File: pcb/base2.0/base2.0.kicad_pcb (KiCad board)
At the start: 4 copper layers, 24 x 24 mm, 32 parts, among them J1 Conn_01x01_Male, J2 Conn_01x01_Male, J3 Conn_01x04_Male, J4 Conn_01x02_Male, U1 STM32G431CBU6, U2 tile, U3 AP2210-33, U4 MPU-9250

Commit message: le update
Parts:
- removed R10, R6, R7, R8, R9: 10k, Resistor_SMD:R_0402_1005Metric
- C9: value 0.1uF -> 100nf
- U4: value MPU-9250 -> LSM6DS3; footprint Sensor_Motion:InvenSense_QFN-24_3x3mm_P0.4mm -> Package_LGA:LGA-14_3x2.5mm_P0.5mm_LayoutBorder3x4y
- moved C9 1.65 mm to (202.9, 101.1), turned to 180 degrees
- moved C8 1.01 mm to (204.9, 101.1), turned to 180 degrees
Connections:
- C8 pad 1: GND -> +3V3
- C8 pad 2: +3V3 -> GND
- C9 pad 1: Net-(C9-Pad1) -> GND
- C9 pad 2: GND -> +3V3
- U4 pad 1: +3V3 -> GND
- U4 pad 10: Net-(C9-Pad1) -> Net-(U4-Pad10)
- U4 pad 12: Net-(R10-Pad1) -> +3V3
- U4 pad 13: +3V3 -> I2C_SCL
- U4 pad 14: (no net) -> I2C_SDA
- U4 pad 2: (no net) -> GND
- U4 pad 3: (no net) -> GND
- U4 pad 4: (no net) -> Net-(U4-Pad4)
- U4 pad 5: (no net) -> +3V3
- U4 pad 6: (no net) -> GND
- U4 pad 7: I2C_SCL -> GND
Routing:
- net GND: track 23.8 -> 30.2 mm, vias 5 -> 14
- net I2C_SCL: track 15.0 -> 18.7 mm
- net Net-(R10-Pad1): track 2.86 -> 0.00 mm
- net I2C_SDA: track 18.0 -> 15.5 mm
- net Net-(U4-Pad11): track 2.31 -> 0.00 mm
- net Net-(C9-Pad1): track 2.27 -> 0.00 mm
- net Net-(R8-Pad2): track 1.83 -> 0.00 mm
- net Net-(U4-Pad9): track 1.80 -> 0.00 mm
- net Net-(R6-Pad2): track 1.57 -> 0.00 mm
- net +3V3: track 40.3 -> 40.5 mm, vias 14 -> 13

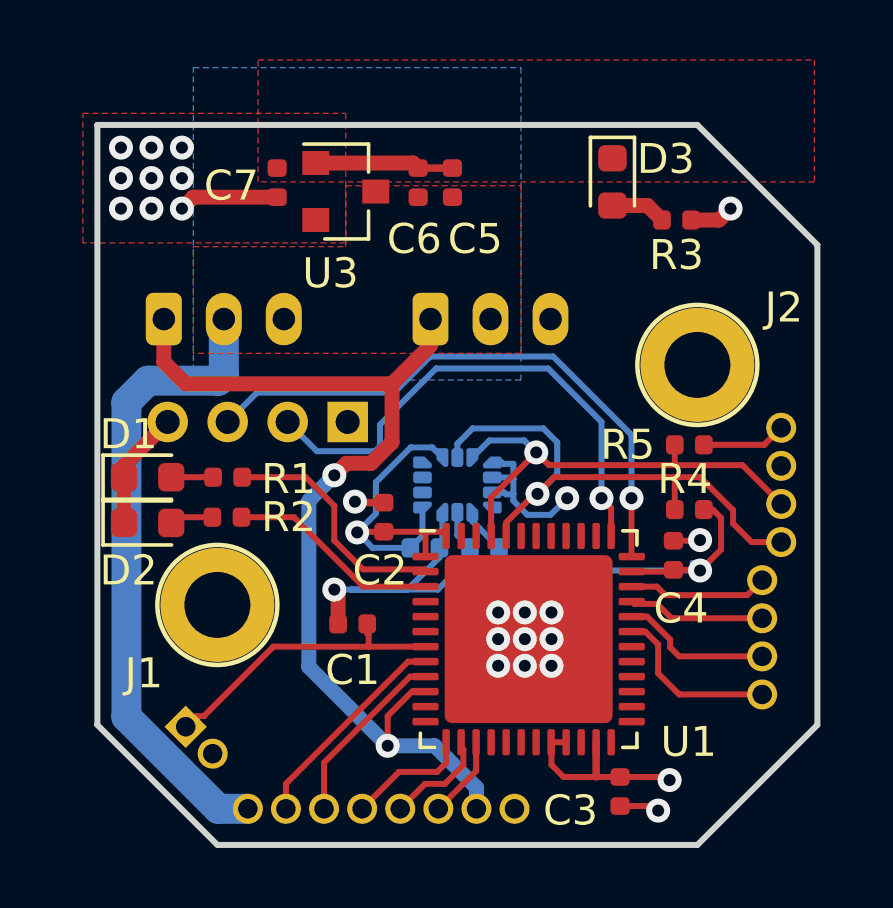
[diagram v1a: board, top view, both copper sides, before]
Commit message: Small changes to base pcb
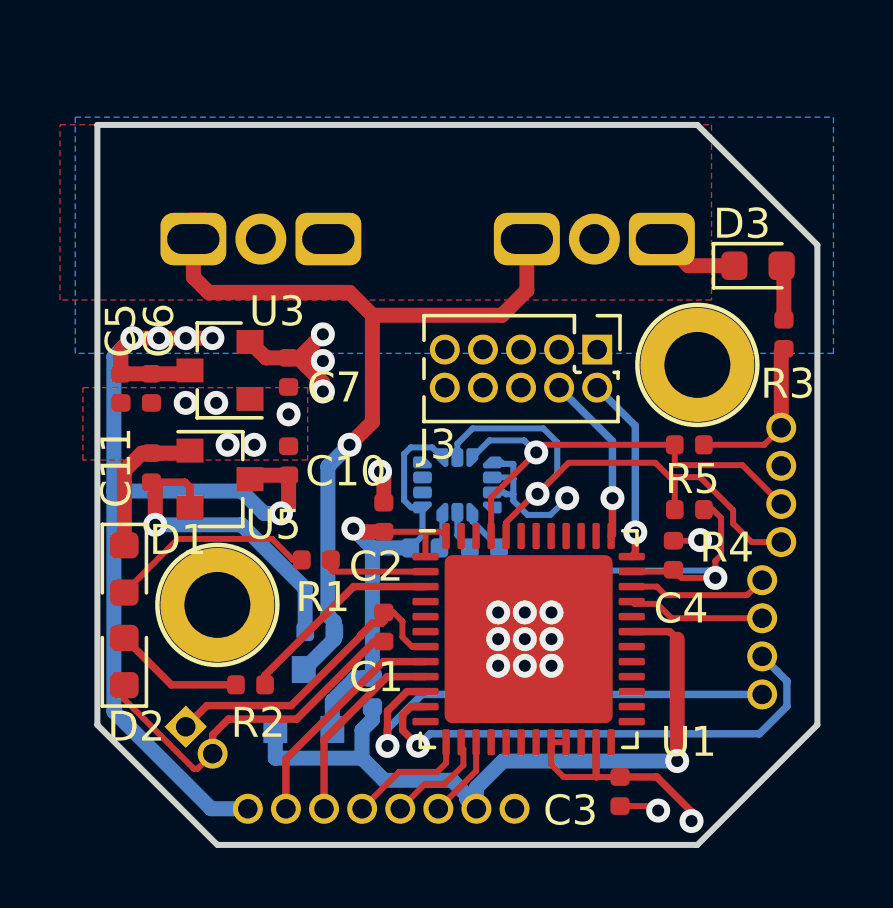
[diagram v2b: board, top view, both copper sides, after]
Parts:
- added C10: 1uf, Capacitor_SMD:C_0402_1005Metric, F.Cu at (198.4, 98.2)
- added C11: 2.2uF, Capacitor_SMD:C_0402_1005Metric, F.Cu at (193.8, 98.4)
- added Q1: BSS123, Package_TO_SOT_SMD:SOT-23, B.Cu at (198.9, 106.2)
- added R6: 10k, Resistor_SMD:R_0402_1005Metric, B.Cu at (199.4, 103.9)
- added R7: 10k, Resistor_SMD:R_0402_1005Metric, B.Cu at (201.2, 105.9)
- added U5: AP2210-5, Package_TO_SOT_SMD:SOT-23, F.Cu at (196.1, 98.8)
- J3: value Conn_01x04_Male -> Conn_ARM_JTAG_SWD_10; footprint Connector_PinHeader_2.00mm:PinHeader_1x04_P2.00mm_Vertical -> Connector_PinHeader_1.27mm:PinHeader_2x05_P1.27mm_Vertical; moved to F.Cu
- S1, S2: footprint Connector_JST:JST_PH_S3B-PH-K_1x03_P2.00mm_Horizontal -> tile:jst_bus_horizontal
- moved C5 13.0 mm to (192.8, 95.8), turned to 270 degrees
- moved C6 11.2 mm to (193.8, 95.8), turned to 270 degrees
- moved J3 8.66 mm to (208.7, 94.5), turned to 270 degrees
- moved S2 7.92 mm to (210.6, 90.8), turned to 180 degrees
- moved U3 7.29 mm to (196.1, 95.2), turned to 180 degrees
- moved C7 6.34 mm to (198.4, 95.2), turned to 270 degrees
- moved S1 5.87 mm to (199.4, 90.8), turned to 180 degrees
- moved R2 5.64 mm to (197.1, 105.7)
- moved D3 5.60 mm to (214.0, 91.7), turned to 0 degrees
- moved R3 5.23 mm to (214.9, 94.0), turned to 90 degrees
- moved D2 4.69 mm to (192.9, 104.9), turned to 90 degrees
- moved R1 4.04 mm to (199.3, 101.5)
- moved D1 3.15 mm to (192.9, 101.8), turned to 270 degrees
- moved C1 1.04 mm to (201.5, 103.7), turned to 270 degrees
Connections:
- J3 pad 2: JTCK-SWCLI -> JTMS-SWDIO
- J3 pad 3: JTMS-SWDIO -> GND
- J3 pad 4: GND -> JTCK-SWCLI
- S1 pad 1: USART2 -> GND
- S1 pad 3: GND -> USART1_5
- S2 pad 1: USART2 -> GND
- S2 pad 3: GND -> USART1_5
- U1 pad 10: USART2 -> USART2_TX
- U1 pad 11: Net-(U1-Pad11) -> USART2_RX
- U1 pad 31: USART1_TX -> USART1_3
- U1 pad 32: USART1_RX -> Net-(U1-Pad32)
- U1 pad 44: I2C_SCL -> Net-(U1-Pad44)
- U1 pad 46: Net-(U1-Pad46) -> I2C_SCL
- U2 pad 10: USART2 -> USART1_3
- U2 pad 7: USART1_RX -> USART2_RX
- U2 pad 8: USART1_TX -> USART2_TX
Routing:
- net USART2: track 33.6 -> 0.00 mm, vias 2 -> 0
- net USART1_5: track 0.00 -> 28.4 mm, vias 0 -> 1
- net USART1_3: track 0.00 -> 23.7 mm, vias 0 -> 1
- net USART2_RX: track 0.00 -> 17.0 mm, vias 0 -> 1
- net USART2_TX: track 0.00 -> 16.2 mm, vias 0 -> 1
- net +3V3: track 40.5 -> 53.9 mm, vias 13 -> 6
- net JTMS-SWDIO: track 19.5 -> 6.21 mm
- net VCC: track 21.3 -> 33.6 mm, vias 0 -> 5
- net JTCK-SWCLI: track 17.1 -> 5.70 mm
- net +5V: track 0.00 -> 10.8 mm, vias 0 -> 1
- net USART1_TX: track 5.78 -> 0.00 mm
- net Net-(D1-Pad2): track 1.39 -> 6.95 mm
- net USART1_RX: track 5.05 -> 0.00 mm
- net LED_2: track 8.12 -> 3.50 mm
- net GND: track 30.2 -> 34.0 mm, vias 14 -> 18
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- added copper zone on In2.Cu, net VCC
- removed copper zone on F.Cu, net +3V3
- removed copper zone on F.Cu, net VCC

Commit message: fixed i2c lines on base2.0 pcb
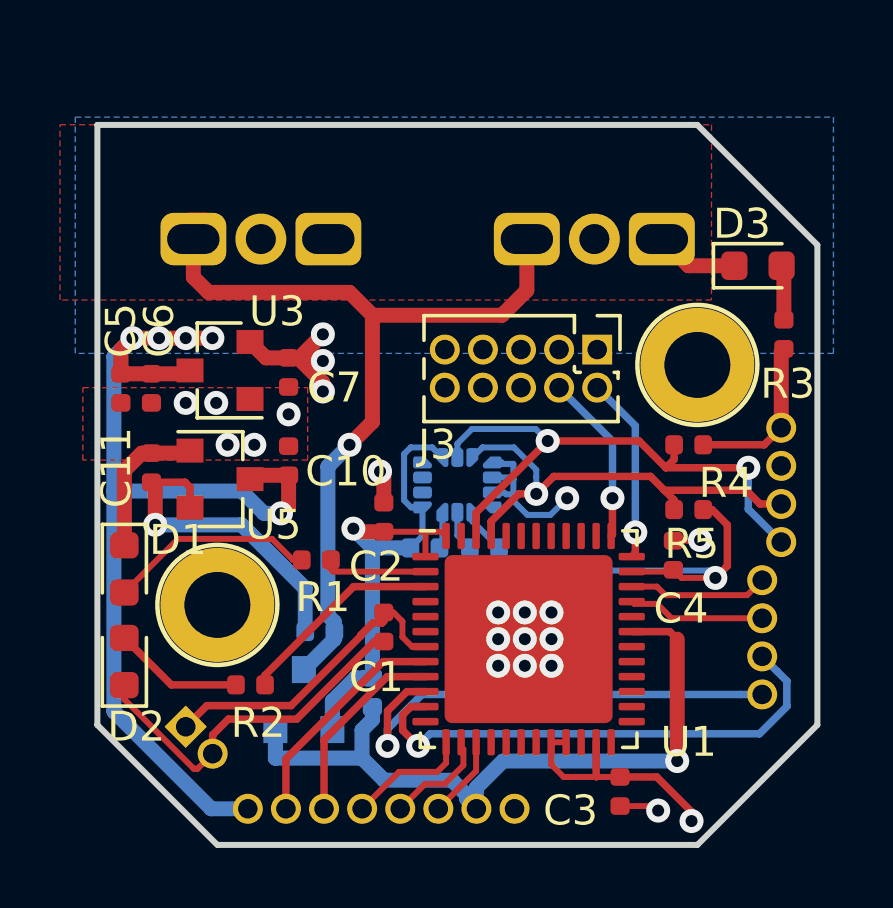
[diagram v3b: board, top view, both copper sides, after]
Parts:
- moved R4 2.16 mm to (211.7, 97.7)
- moved R5 2.16 mm to (211.7, 99.8)
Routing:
- net I2C_SCL: track 19.1 -> 18.9 mm, vias 1 -> 2

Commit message: added another pcbs
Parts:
- C8, C9, Q1, R6, R7, U4: moved to F.Cu
- moved R4 5.35 mm to (206.4, 97.3), turned to 90 degrees
- moved C1 5.28 mm to (198.4, 108.0)
- moved R6 4.34 mm to (200.6, 99.7)
- moved R1 4.31 mm to (200.4, 105.7)
- moved Q1 4.21 mm to (200.0, 102.1), turned to 0 degrees
- moved C9 4.00 mm to (206.5, 99.3), turned to 270 degrees
- moved R2 3.45 mm to (200.4, 106.7)
- moved C2 2.87 mm to (203.6, 102.1), turned to 180 degrees
- moved U1 2.57 mm to (208.9, 104.5)
- moved R5 2.49 mm to (210.5, 97.7)
- moved C8 2.21 mm to (202.7, 101.1)
- moved C4 1.86 mm to (212.1, 99.7), turned to 180 degrees
- moved R7 1.79 mm to (200.0, 104.5), turned to 180 degrees
- moved J3 0.76 mm to (208.7, 93.7)
- moved C3 0.68 mm to (210.1, 109.5), turned to 180 degrees
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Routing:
- net +3V3: track 54.1 -> 47.3 mm
- net USART1_5: track 28.4 -> 23.7 mm, vias 1 -> 0
- net I2C_SDA: track 15.3 -> 19.4 mm
- net GND: track 34.0 -> 30.1 mm, vias 18 -> 14
- net +5V: track 10.8 -> 7.04 mm, vias 1 -> 0
- net Net-(D2-Pad2): track 4.37 -> 8.09 mm
- net MOSI: track 2.74 -> 6.30 mm
- net USART2_TX: track 16.2 -> 12.7 mm
- net LED_2: track 3.50 -> 6.77 mm
- net JTCK-SWCLI: track 5.70 -> 8.48 mm
- net FDCAN_RX: track 4.58 -> 1.89 mm
- net FDCAN_TX: track 4.88 -> 2.26 mm
- net JTMS-SWDIO: track 6.21 -> 8.59 mm
- net MISO: track 3.51 -> 5.62 mm
- net SCK: track 4.12 -> 6.11 mm
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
